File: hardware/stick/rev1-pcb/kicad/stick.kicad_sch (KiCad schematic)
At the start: 0 parts

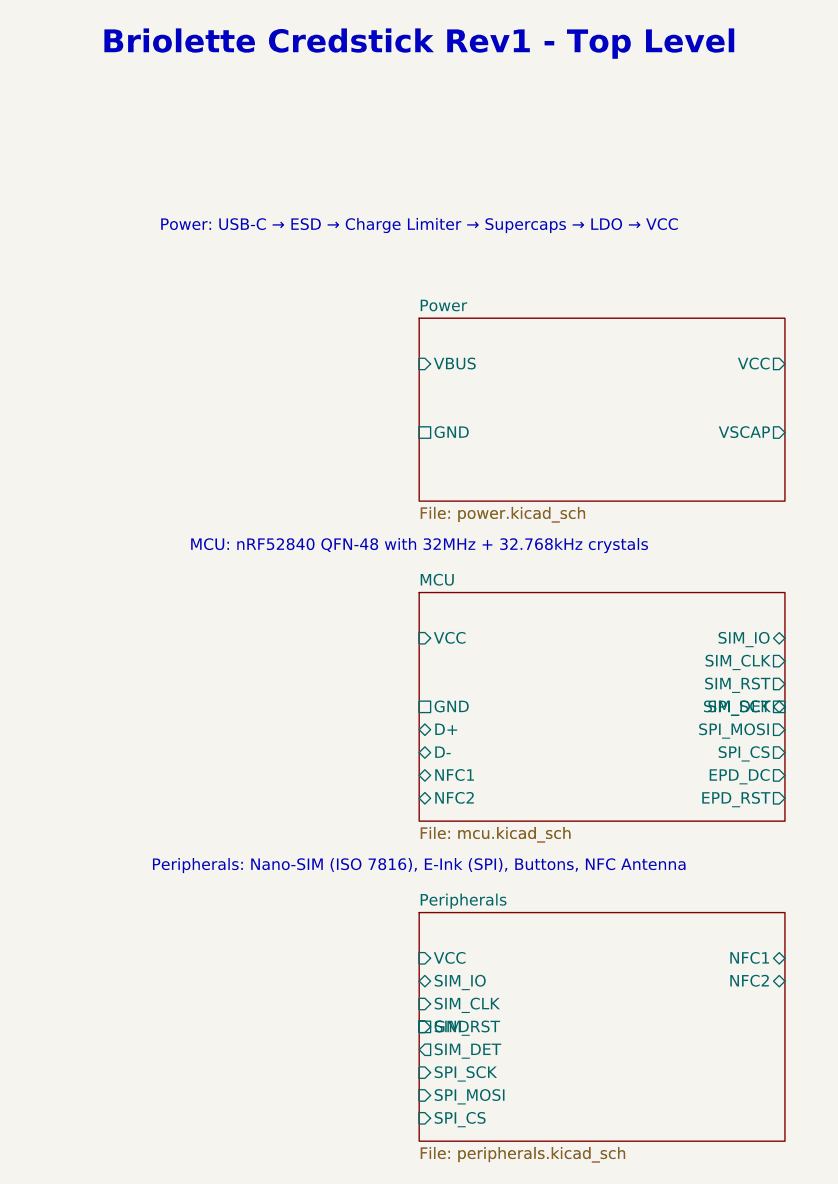
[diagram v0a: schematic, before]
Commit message: Fix DOA-causing issues in credstick and relay PCB designs
Critical fixes:
- HASL→ENIG copper finish on both PCBs (QFN pads need flat surface)
- Replace stale ATECC608B footprint with Nano-SIM connector on credstick PCB
- Fix NFC antenna spirals: closed rectangles→continuous spiral with crossover vias
- Fix TCA8418/SW3 component overlap at (-20,-15) on relay PCB
- Add missing inter-sheet pins (EPD_BUSY, BTN_L/R, LED, VSCAP_SENSE) to credstick top-level
- Fix button footprints (SW_SPST_PTS810→SW_SPST_3x3mm) to match schematic
- Replace stale I2C nets (SDA/SCL) with SIM interface nets
- Fix nRF52840 package description in both BOMs (aQFN-73 7x7→QFN-48 6x6)
- Remove ATECC608B reference from credstick BOM sourcing guide

https://claude.ai/code/session_01TM1rFxbipYtvAkh4Vt7My7
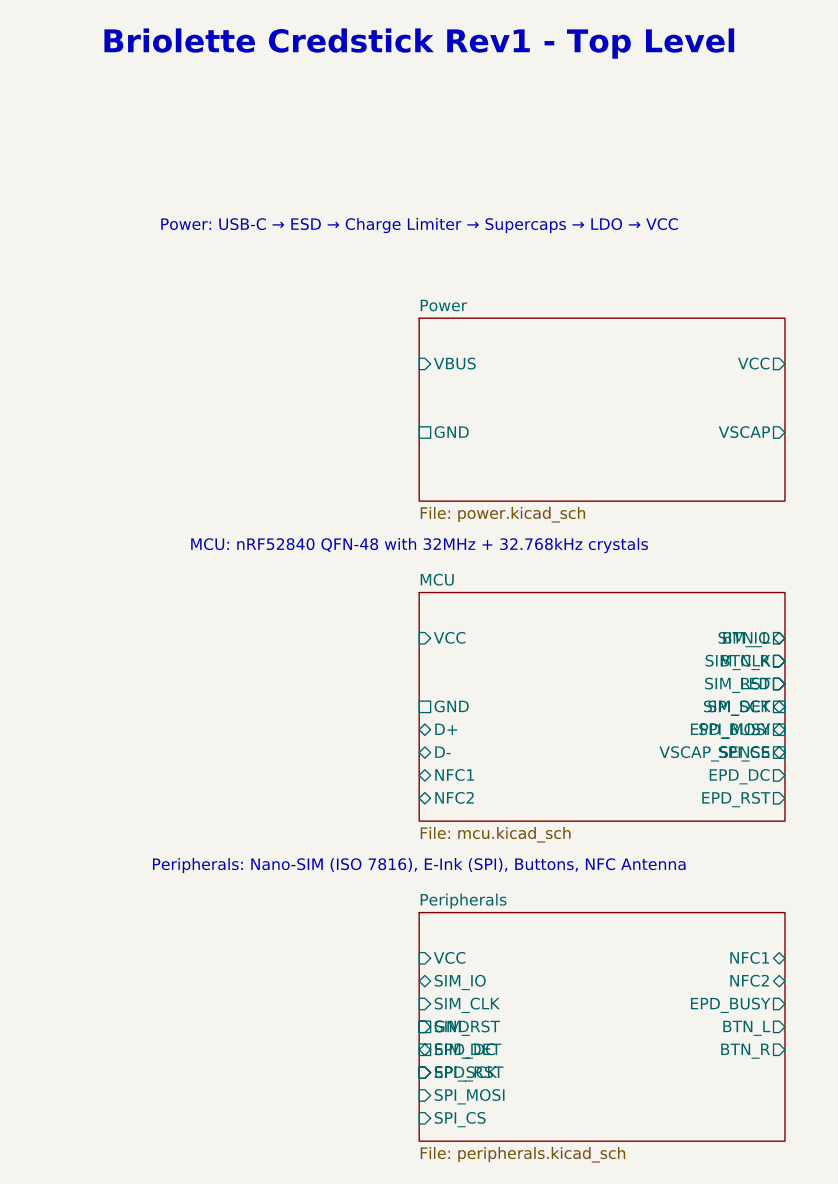
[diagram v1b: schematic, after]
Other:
- sheet MCU ports: added BTN_L, BTN_R, EPD_BUSY, LED, VSCAP_SENSE; removed none
- sheet Peripherals ports: added BTN_L, BTN_R, EPD_BUSY, EPD_DC, EPD_RST; removed none
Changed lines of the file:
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@@
       (effects (font (size 1.27 1.27)) (justify left))
+    )
+    (pin "BTN_L" output
+      (at 66.04 86.36 0)
+      (effects (font (size 1.27 1.27)) (justify right))
+    )
+    (pin "BTN_R" output
+      (at 66.04 88.9 0)
+      (effects (font (size 1.27 1.27)) (justify right))
+    )
+    (pin "LED" output
+      (at 66.04 91.44 0)
+      (effects (font (size 1.27 1.27)) (justify right))
+    )
+    (pin "EPD_BUSY" input
+      (at 66.04 96.52 0)
+      (effects (font (size 1.27 1.27)) (justify right))
+    )
+    (pin "VSCAP_SENSE" input
+      (at 66.04 99.06 0)
+      (effects (font (size 1.27 1.27)) (justify right))
     )
   )
@@
       (effects (font (size 1.27 1.27)) (justify left))
     )
+    (pin "EPD_DC" input
+      (at 25.4 132.08 180)
+      (effects (font (size 1.27 1.27)) (justify left))
+    )
+    (pin "EPD_RST" input
+      (at 25.4 134.62 180)
+      (effects (font (size 1.27 1.27)) (justify left))
+    )
+    (pin "EPD_BUSY" output
+      (at 66.04 127 0)
+      (effects (font (size 1.27 1.27)) (justify right))
+    )
+    (pin "BTN_L" output
+      (at 66.04 129.54 0)
+      (effects (font (size 1.27 1.27)) (justify right))
+    )
+    (pin "BTN_R" output
+      (at 66.04 132.08 0)
+      (effects (font (size 1.27 1.27)) (justify right))
+    )
     (pin "NFC1" bidirectional
